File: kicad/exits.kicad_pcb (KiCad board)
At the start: 2 copper layers, 39.3 x 106.5 mm, 65 parts, among them J1 PJ301M12, J12 Euro power header, J13 SJ-63083A, J14 PJ301M12, J2 PJ301M12, J3 PJ301M12, J4 PJ301M12, U1 TL074, U2 RC4580

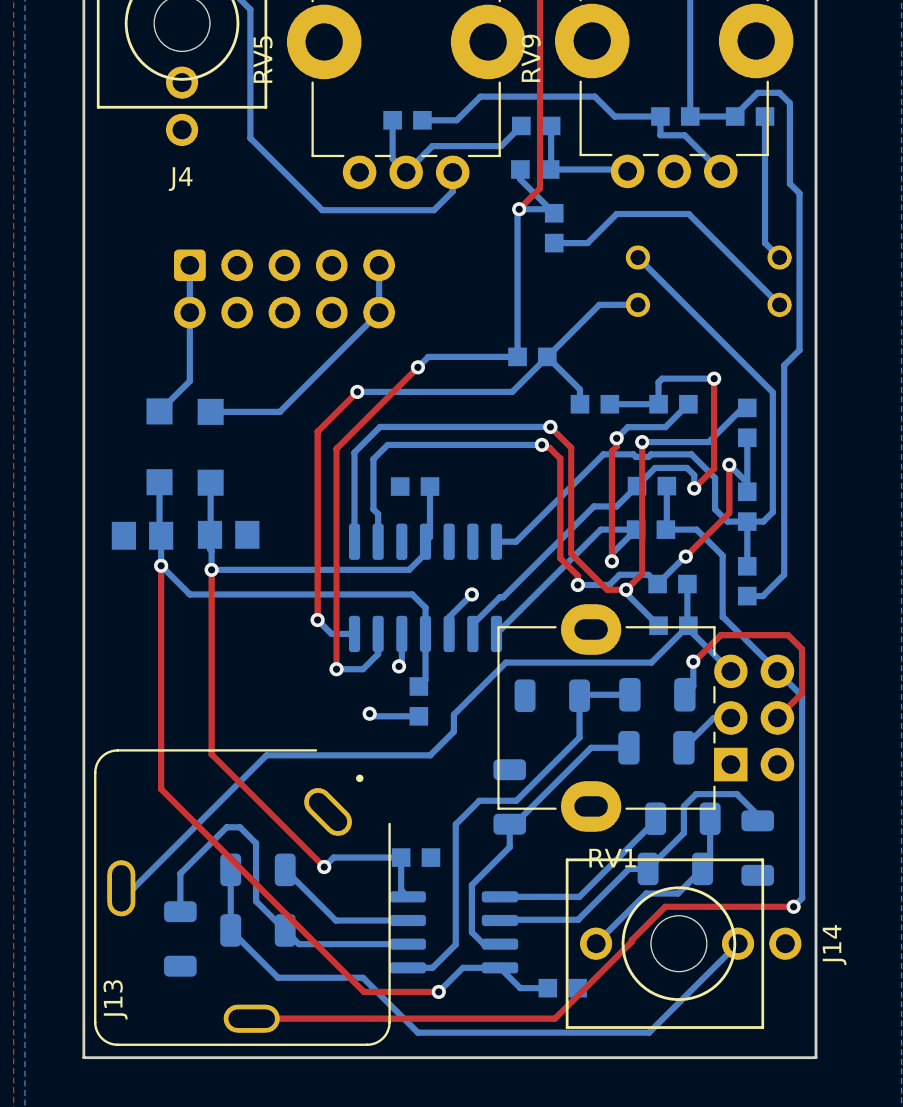
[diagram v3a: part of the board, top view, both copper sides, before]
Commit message: add panel outline, tweak R values, dips -> headers
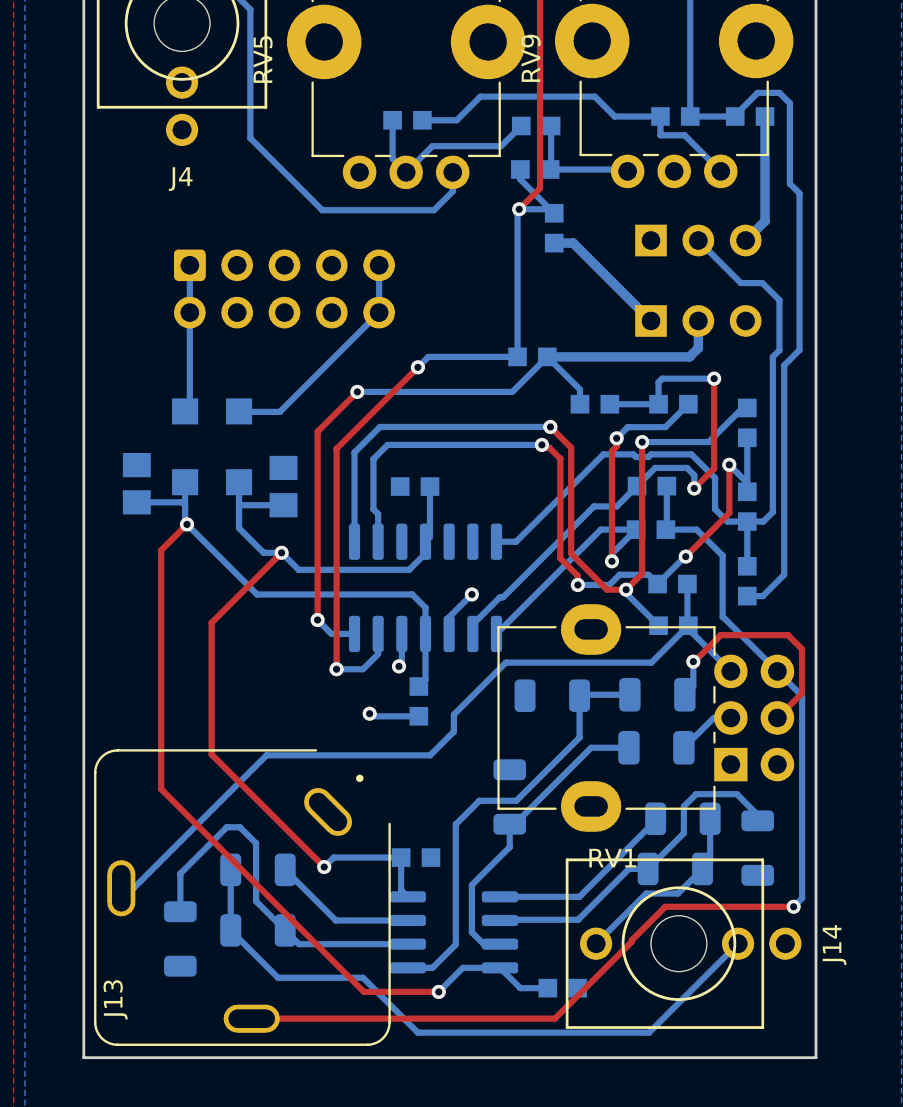
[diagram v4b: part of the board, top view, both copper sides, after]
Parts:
- removed S1: ADP0204, SamacSys_Parts:ADP0204
- added J5: Attenuator Jumper 1, Connector_PinHeader_2.54mm:PinHeader_1x03_P2.54mm_Vertical, B.Cu at (44.7, 88.2)
- added J6: Attenuator Jumper 1, Connector_PinHeader_2.54mm:PinHeader_1x03_P2.54mm_Vertical, B.Cu at (44.7, 92.5)
- R23, R24: value 2.2K -> 10K
- R25, R26: value 10k -> 1K
- R29, R30: value 1k -> 470
- moved C5 3.92 mm to (25.0, 101.4), turned to 90 degrees
- moved C6 2.81 mm to (17.1, 101.2), turned to -90 degrees
- moved D1 1.52 mm to (22.6, 99.3)
- moved D2 1.37 mm to (19.7, 99.3)
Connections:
- RV1 pad 1: unconnected-(RV1-Pad1) -> GND
- RV1 pad 4: unconnected-(RV1-Pad4) -> GND
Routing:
- net Net-(R19-Pad2): track 14.8 -> 6.93 mm
- net Net-(R20-Pad2): track 35.7 -> 39.4 mm
- net -12V: track 62.1 -> 65.0 mm
- net +12V: track 44.6 -> 46.8 mm
- net Net-(D1-Pad2): track 13.8 -> 12.3 mm
- net Net-(R18-Pad2): track 7.89 -> 7.09 mm
- net Net-(D2-Pad1): track 8.52 -> 7.95 mm
- net Net-(R17-Pad2): track 38.6 -> 39.2 mm

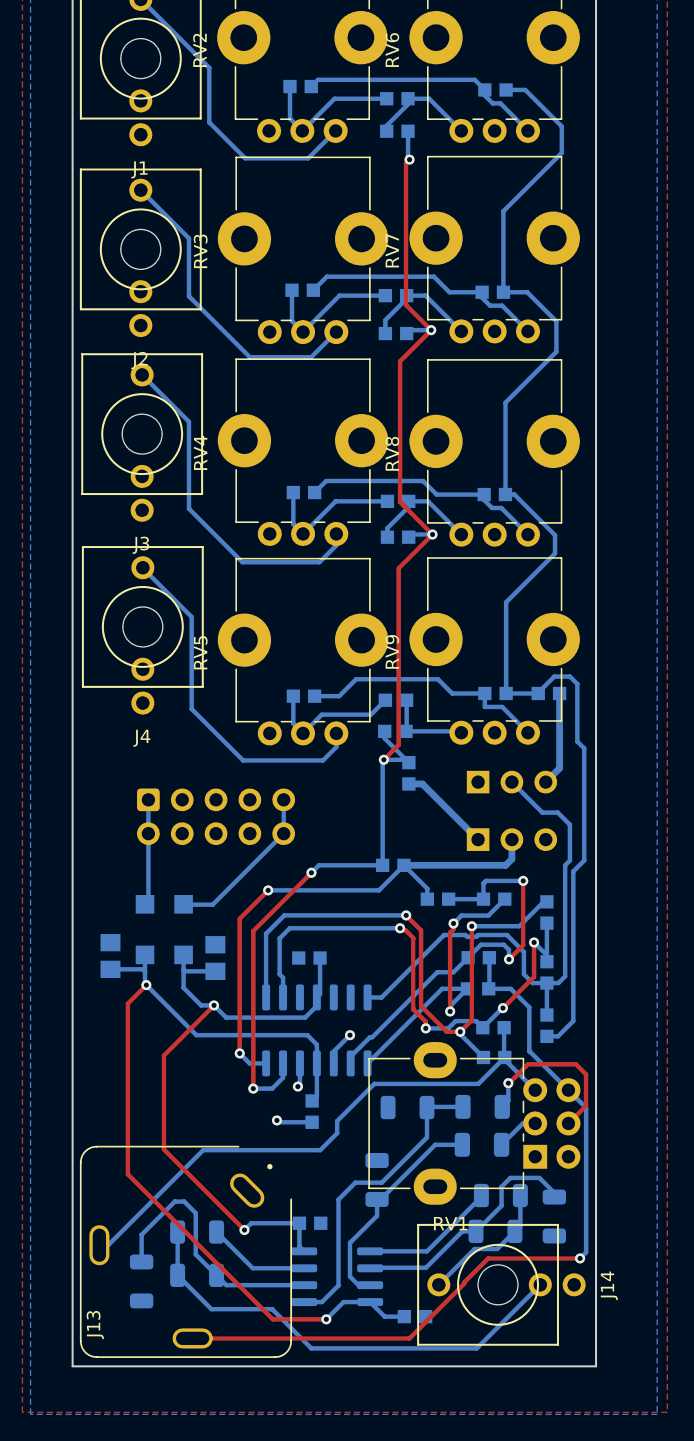
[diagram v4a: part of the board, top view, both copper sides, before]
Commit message: Switched to non-inverting amp config, tweaked values
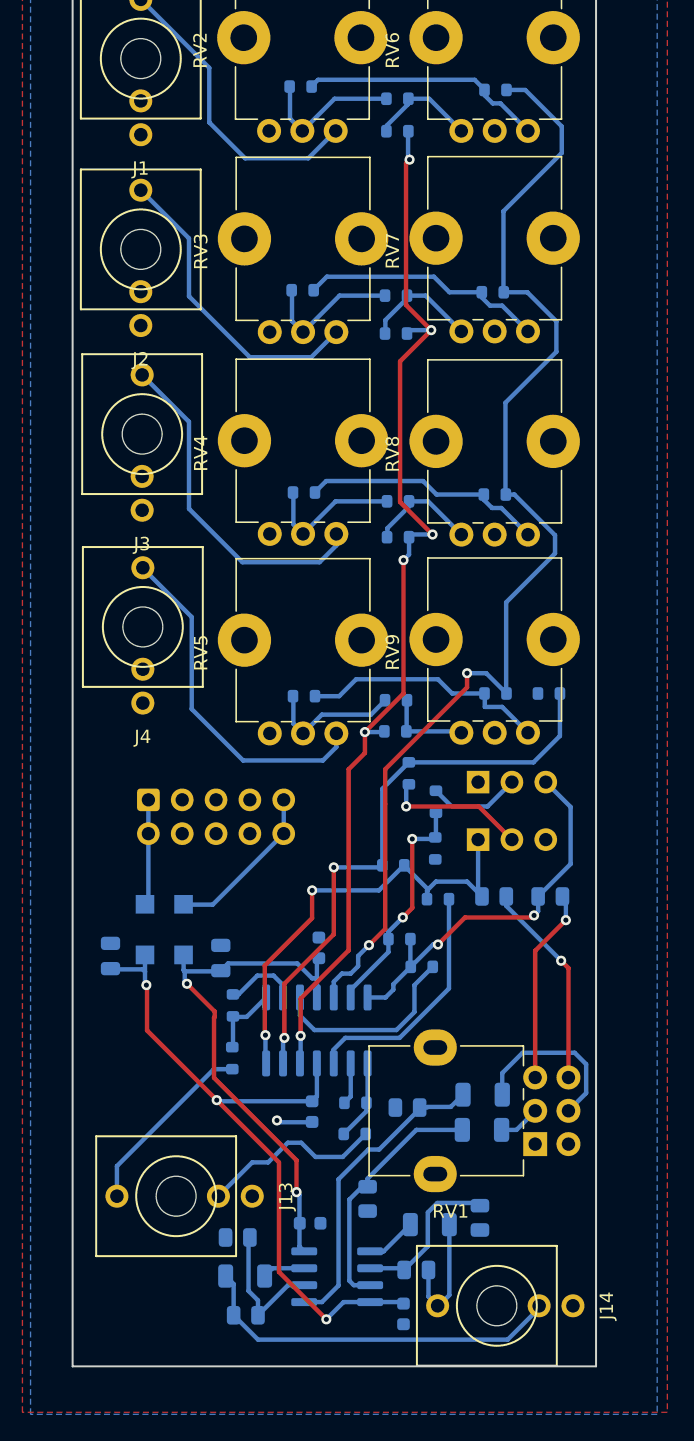
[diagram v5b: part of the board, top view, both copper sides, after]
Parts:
- removed C3, C4: 22p, nearness:0603
- added R35: 100K, Resistor_SMD:R_0805_2012Metric, B.Cu at (50.1, 96.8)
- added R36: 100K, Resistor_SMD:R_0805_2012Metric, B.Cu at (45.9, 96.8)
- added R37: 1K, Resistor_SMD:R_0603_1608Metric, B.Cu at (41.5, 93.2)
- added R38: 20K, Resistor_SMD:R_0603_1608Metric, B.Cu at (41.6, 89.7)
- C10, C7, C8, C9: footprint nearness:0603 -> Capacitor_SMD:C_0603_1608Metric
- C5, C6: footprint nearness:0805 -> Capacitor_SMD:C_0805_2012Metric
- J13: value SJ-63083A -> PJ301M12; footprint Connector:CUI_SJ-63083A -> nearness:PJ301M12
- J6: value Attenuator Jumper 1 -> Attenuator Jumper 2
- R1, R10, R11, R12, R13, R14, R2, R3, R31, R32, R4, R5, R6, R7, R8, R9: value R_Small -> 100K; footprint nearness:0603 -> Resistor_SMD:R_0603_1608Metric
- R15, R16: value 100k -> 100K; footprint Resistor_SMD:R_1206_3216Metric -> Resistor_SMD:R_0805_2012Metric
- R17, R19, R20: value 100k -> 20K; footprint nearness:0603 -> Resistor_SMD:R_0603_1608Metric
- R18: value 100k -> 1K; footprint nearness:0603 -> Resistor_SMD:R_0603_1608Metric
- R21, R22, R27, R28: value 100k -> 10K; footprint nearness:0603 -> Resistor_SMD:R_0603_1608Metric
- R23, R24, R25, R26: footprint Resistor_SMD:R_1206_3216Metric -> Resistor_SMD:R_0805_2012Metric
- R29, R30: footprint nearness:0603 -> Resistor_SMD:R_0603_1608Metric
- RV1: value 50k A -> B10K
- RV2, RV3, RV4, RV5: value Volume -> 20K
- RV6, RV7, RV8, RV9: value Pan -> 10K
- moved R29 19.7 mm to (26.3, 108.9), turned to -90 degrees
- moved R27 19.6 mm to (26.3, 105.0), turned to -90 degrees
- moved R28 14.3 mm to (35.5, 112.3)
- moved R30 14.3 mm to (35.5, 114.6)
- moved R17 12.8 mm to (38.8, 100.0), turned to 0 degrees
- moved R21 9.41 mm to (40.5, 102.1), turned to 0 degrees
- moved R24 7.93 mm to (26.7, 122.4), turned to 0 degrees
- moved R25 6.61 mm to (40.1, 124.8)
- moved R33 5.76 mm to (41.1, 121.4)
- moved R23 5.59 mm to (44.9, 120.9)
- moved R34 4.89 mm to (27.2, 125.3)
- moved R26 4.73 mm to (27.3, 128.2)
- moved J13 4.25 mm to (22.0, 119.3)
- moved R15 1.59 mm to (36.4, 119.5), turned to 90 degrees
- moved J14 1.58 mm to (46.1, 127.5)
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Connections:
- J13 pad 3: Rout -> LLineOut
- J5 pad 2: Net-(R17-Pad2) -> Net-(J5-Pad2)
- J5 pad 3: Net-(R18-Pad2) -> Lout
- J6 pad 1: Net-(R19-Pad2) -> Rout
- J6 pad 2: Net-(R20-Pad2) -> Net-(J6-Pad2)
- R17 pad 1: /LeftMix -> Net-(R17-Pad1)
- R17 pad 2: Net-(R17-Pad2) -> Lout
- R18 pad 1: /LeftMix -> GND
- R18 pad 2: Net-(R18-Pad2) -> Net-(U1-Pad13)
- R19 pad 1: /RightMix -> Net-(U1-Pad13)
- R19 pad 2: Net-(R19-Pad2) -> Net-(J6-Pad2)
- R20 pad 1: /RightMix -> Net-(U1-Pad13)
- R20 pad 2: Net-(R20-Pad2) -> Rout
- R21 pad 1: Net-(R17-Pad2) -> Lout
- R21 pad 2: Net-(C3-Pad1) -> Net-(R21-Pad2)
- R22 pad 1: Net-(R20-Pad2) -> Rout
- R22 pad 2: Net-(C4-Pad1) -> Net-(R22-Pad2)
- R27 pad 1: Net-(C3-Pad1) -> Net-(U1-Pad2)
- R27 pad 2: Lout -> Net-(R27-Pad2)
- R28 pad 1: Net-(C4-Pad1) -> Net-(U1-Pad9)
- R28 pad 2: Rout -> Net-(R28-Pad2)
- R29 pad 1: Net-(C3-Pad2) -> Net-(R27-Pad2)
- R29 pad 2: Lout -> LLineOut
- R30 pad 1: Net-(C4-Pad2) -> Net-(R28-Pad2)
- R30 pad 2: Rout -> RLineOut
- RV1 pad 3: Lout -> Net-(R35-Pad1)
- RV1 pad 6: Rout -> Net-(R36-Pad1)
- U1 pad 1: Net-(C3-Pad2) -> Net-(R27-Pad2)
- U1 pad 10: GND -> Net-(R22-Pad2)
- U1 pad 12: GND -> /RightMix
- U1 pad 13: /RightMix -> Net-(U1-Pad13)
- U1 pad 14: Net-(R20-Pad2) -> Rout
- U1 pad 2: Net-(C3-Pad1) -> Net-(U1-Pad2)
- U1 pad 3: GND -> Net-(R21-Pad2)
- U1 pad 5: GND -> /LeftMix
- U1 pad 6: unconnected-(U1-Pad6) -> Net-(R17-Pad1)
- U1 pad 7: Net-(R17-Pad2) -> Lout
- U1 pad 8: Net-(C4-Pad2) -> Net-(R28-Pad2)
- U1 pad 9: Net-(C4-Pad1) -> Net-(U1-Pad9)
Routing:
- net Net-(C3-Pad2): track 44.0 -> 0.00 mm, vias 3 -> 0
- net Net-(U1-Pad13): track 0.00 -> 43.9 mm, vias 0 -> 2
- net Net-(R20-Pad2): track 39.4 -> 0.00 mm, vias 2 -> 0
- net Net-(C3-Pad1): track 39.4 -> 0.00 mm, vias 4 -> 0
- net Net-(R17-Pad2): track 39.2 -> 0.00 mm
- net Net-(C4-Pad1): track 29.4 -> 0.00 mm, vias 2 -> 0
- net Net-(C4-Pad2): track 23.4 -> 0.00 mm, vias 2 -> 0
- net Rout: track 58.4 -> 35.4 mm, vias 1 -> 2
- net Net-(R17-Pad1): track 0.00 -> 17.5 mm, vias 0 -> 2
- net Net-(R22-Pad2): track 0.00 -> 17.3 mm
- net Net-(R36-Pad1): track 0.00 -> 15.5 mm, vias 0 -> 1
- net Net-(R21-Pad2): track 0.00 -> 14.9 mm
- net Net-(R35-Pad1): track 0.00 -> 14.7 mm, vias 0 -> 1
- net /RightMix: track 94.8 -> 80.8 mm
- net LLineOut: track 0.00 -> 13.9 mm
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
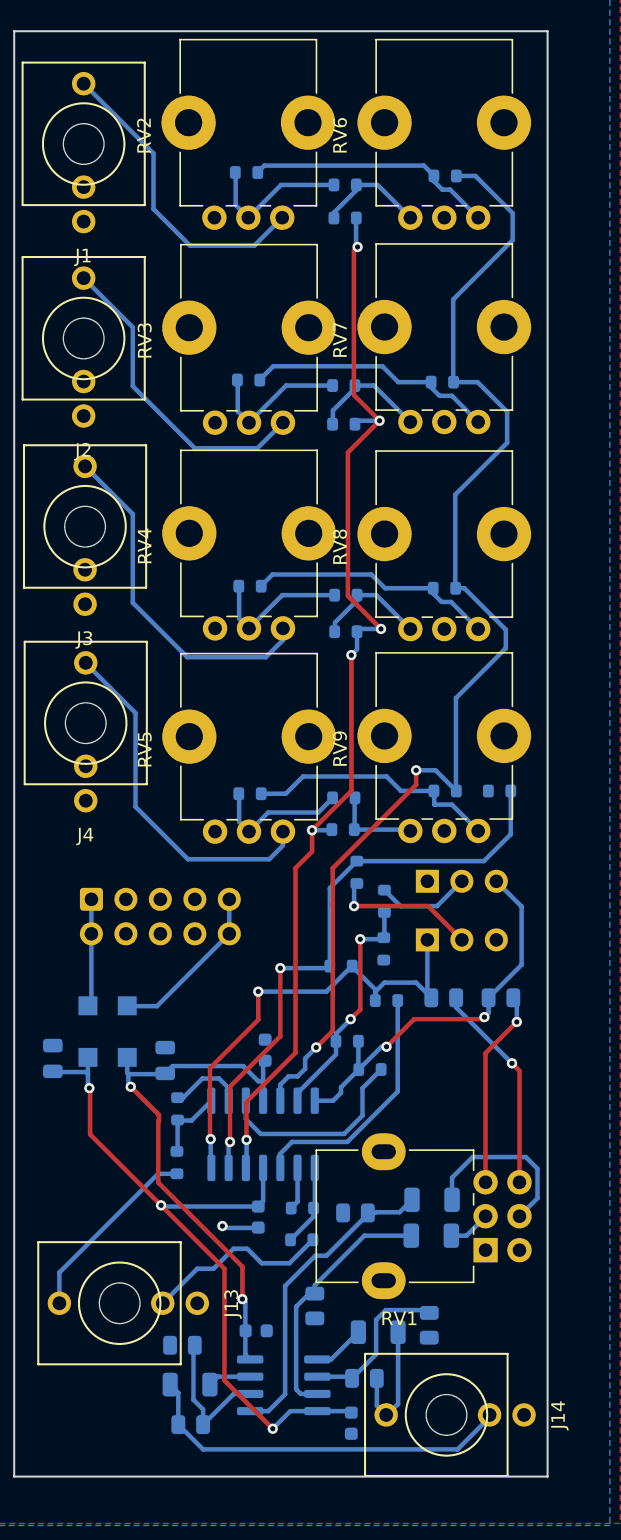
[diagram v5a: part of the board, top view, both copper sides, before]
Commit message: Switched to current mixing, updated pcb
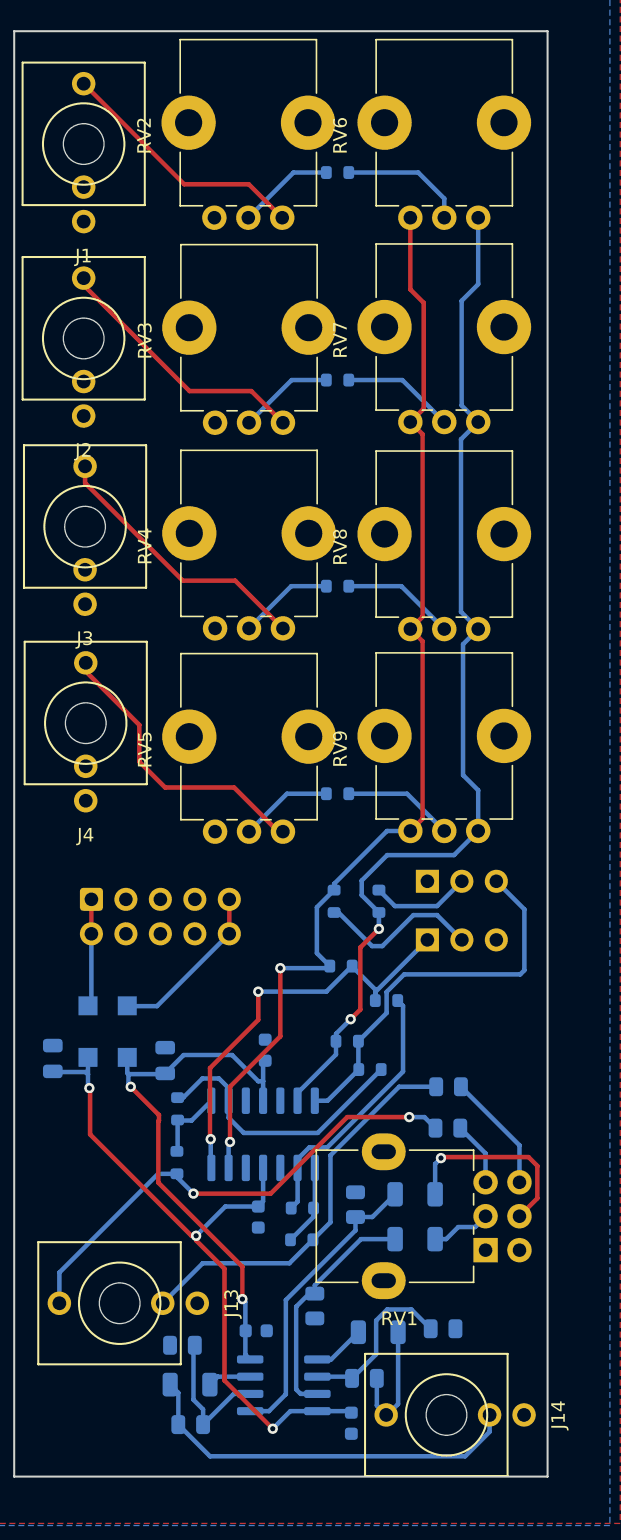
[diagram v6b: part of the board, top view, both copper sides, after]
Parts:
- removed R10, R11, R12, R13, R14, R2, R31, R32, R4, R6, R8, R9: 100K, Resistor_SMD:R_0603_1608Metric
- removed R18, R37: 1K, Resistor_SMD:R_0603_1608Metric
- R1, R3, R5, R7: value 100K -> 50K
- R17, R20: value 20K -> 51K
- R19, R38: value 20K -> 100K
- RV2, RV3, RV4, RV5: value 20K -> 10K Vol
- moved R35 10.4 mm to (46.2, 106.4)
- moved R1 6.71 mm to (38.1, 36.0)
- moved R36 6.56 mm to (46.3, 103.3)
- moved R3 6.55 mm to (38.1, 51.3)
- moved R5 6.45 mm to (38.1, 66.4)
- moved R7 6.45 mm to (38.1, 81.7)
- moved R19 2.71 mm to (37.8, 89.7)
- moved C2 1.31 mm to (43.8, 111.3)
- moved C1 1.22 mm to (43.8, 114.6)
- moved R23 1.05 mm to (45.9, 121.2), turned to 180 degrees
- moved R16 0.61 mm to (39.4, 112.0), turned to -90 degrees
- moved R38 0.41 mm to (41.1, 89.7)
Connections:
- J5 pad 3: Lout -> Net-(J5-Pad3)
- J6 pad 1: Rout -> Net-(J6-Pad1)
- R17 pad 1: Net-(R17-Pad1) -> /LeftMix
- R17 pad 2: Lout -> Net-(J5-Pad3)
- R19 pad 1: Net-(U1-Pad13) -> /RightMix
- R20 pad 1: Net-(U1-Pad13) -> /RightMix
- R20 pad 2: Rout -> Net-(J6-Pad1)
- R21 pad 1: Lout -> Net-(J5-Pad3)
- R22 pad 1: Rout -> Net-(J6-Pad1)
- R27 pad 1: Net-(U1-Pad2) -> Net-(R21-Pad2)
- R28 pad 1: Net-(U1-Pad9) -> Net-(R22-Pad2)
- R3 pad 2: Net-(R11-Pad1) -> Net-(R3-Pad2)
- R35 pad 2: Lout -> LLineOut
- R36 pad 2: Rout -> RLineOut
- R38 pad 1: Net-(R17-Pad1) -> /LeftMix
- R5 pad 2: Net-(R13-Pad1) -> Net-(R5-Pad2)
- R7 pad 2: Net-(R31-Pad1) -> Net-(R7-Pad2)
- RV6 pad 1: Net-(R1-Pad2) -> /LeftMix
- RV6 pad 2: GND -> Net-(R1-Pad2)
- RV6 pad 3: Net-(R10-Pad1) -> /RightMix
- RV7 pad 1: Net-(R11-Pad1) -> /LeftMix
- RV7 pad 2: GND -> Net-(R3-Pad2)
- RV7 pad 3: Net-(R12-Pad1) -> /RightMix
- RV8 pad 1: Net-(R13-Pad1) -> /LeftMix
- RV8 pad 2: GND -> Net-(R5-Pad2)
- RV8 pad 3: Net-(R14-Pad1) -> /RightMix
- RV9 pad 1: Net-(R31-Pad1) -> /LeftMix
- RV9 pad 2: GND -> Net-(R7-Pad2)
- RV9 pad 3: Net-(R32-Pad1) -> /RightMix
- U1 pad 10: Net-(R22-Pad2) -> GND
- U1 pad 12: /RightMix -> GND
- U1 pad 13: Net-(U1-Pad13) -> /RightMix
- U1 pad 14: Rout -> Net-(J6-Pad1)
- U1 pad 2: Net-(U1-Pad2) -> Net-(R21-Pad2)
- U1 pad 3: Net-(R21-Pad2) -> GND
- U1 pad 5: /LeftMix -> GND
- U1 pad 6: Net-(R17-Pad1) -> /LeftMix
- U1 pad 7: Lout -> Net-(J5-Pad3)
- U1 pad 9: Net-(U1-Pad9) -> Net-(R22-Pad2)
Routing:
- net Net-(U1-Pad13): track 43.9 -> 0.00 mm, vias 2 -> 0
- net Rout: track 35.4 -> 0.00 mm, vias 2 -> 0
- net Net-(J6-Pad1): track 0.00 -> 32.1 mm, vias 0 -> 2
- net Lout: track 29.3 -> 0.00 mm, vias 2 -> 0
- net Net-(J5-Pad3): track 0.00 -> 29.0 mm
- net LLineOut: track 13.9 -> 36.4 mm, vias 0 -> 2
- net Net-(R31-Pad1): track 18.8 -> 0.00 mm
- net Net-(R11-Pad1): track 18.5 -> 0.00 mm
- net Net-(R13-Pad1): track 18.3 -> 0.00 mm
- net Net-(R17-Pad1): track 17.5 -> 0.00 mm, vias 2 -> 0
- net RLineOut: track 13.9 -> 29.6 mm
- net /LeftMix: track 89.9 -> 76.9 mm
- net Net-(R35-Pad1): track 14.7 -> 4.76 mm, vias 1 -> 0
- net Net-(R1-Pad2): track 18.3 -> 9.24 mm
- net Net-(R12-Pad1): track 8.49 -> 0.00 mm
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
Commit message: added my readme
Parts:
- moved C5 3.79 mm to (29.0, 100.1)
- moved D1 3.30 mm to (25.9, 99.3)
- moved J1 1.86 mm to (19.4, 32.0)
- moved J2 1.20 mm to (19.4, 47.0)
- moved C8 0.64 mm to (31.6, 112.9)
- moved J4 0.42 mm to (19.5, 77.0)
- moved R35 0.30 mm to (46.2, 106.7)
- moved RV6 0.21 mm to (48.5, 39.5)
- moved RV2 0.21 mm to (34.0, 39.5)
- moved RV7 0.15 mm to (48.5, 54.5)
- moved J14 0.13 mm to (46.1, 127.4)
- moved RV3 0.12 mm to (34.0, 54.5)
- moved RV8 0.11 mm to (48.5, 69.5)
- moved RV4 0.09 mm to (34.0, 69.5)
- moved J3 0.08 mm to (19.5, 62.0)
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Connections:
- J5 pad 1: unconnected-(J5-Pad1) -> Net-(J5-Pad1)
- J5 pad 3: Net-(J5-Pad3) -> unconnected-(J5-Pad3)
- R17 pad 2: Net-(J5-Pad3) -> Net-(J5-Pad1)
- R21 pad 1: Net-(J5-Pad3) -> Net-(J5-Pad1)
- U1 pad 7: Net-(J5-Pad3) -> Net-(J5-Pad1)
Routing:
- net Net-(J5-Pad3): track 29.0 -> 0.00 mm
- net Net-(J5-Pad1): track 0.00 -> 21.1 mm, vias 0 -> 1
- net +12V: track 39.7 -> 35.9 mm
- net Net-(D1-Pad2): track 12.2 -> 10.1 mm
- net Net-(J1-Pad3): track 18.7 -> 20.6 mm
- net Net-(J6-Pad1): track 32.1 -> 33.3 mm
- net Net-(J2-Pad3): track 19.4 -> 20.4 mm
- net /LeftMix: track 76.9 -> 76.1 mm
- net Net-(J3-Pad3): track 20.2 -> 20.8 mm
- net Net-(J4-Pad3): track 21.6 -> 21.1 mm
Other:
- board text added: "+12"
- board text added: "<- CC BY-SA 4.0"
- board text added: "Based on ramphands/Exits & sarnesjo/nearness"
- board text added: "MOUTH by Crows Electromusic"
- board text removed: "Exits github.com/ramphands/Exits CC BY-SA 4.0"
